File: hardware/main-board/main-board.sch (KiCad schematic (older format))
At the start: 92 parts, among them J1 BARREL_JACK, J2 CONN_01X10, J3 CONN_01X10, J4 USB_OTG, J5 CONN_02X05, J6 SMA, Q1 DDTD113ZC, Q2 DDTD113ZC, Q3 DDTD113ZC, Q4 DDTD113ZC, Q5 DDTD113ZC, Q6 FDB14N30TM, Q7 DDTD113ZC, Q8 DDTD113ZC, Q9 DDTD113ZC, SW1 SW_Push, SW2 SW_Push, SW3 SW_Push, SW4 SW_Push, SW5 SW_DIP_x01, U1 LD1117S33TR, U2 MAX1771, U3 STM32F302C, U4 FGPMMOPA6H, Y1 8MHz, Y2 32.768kHz

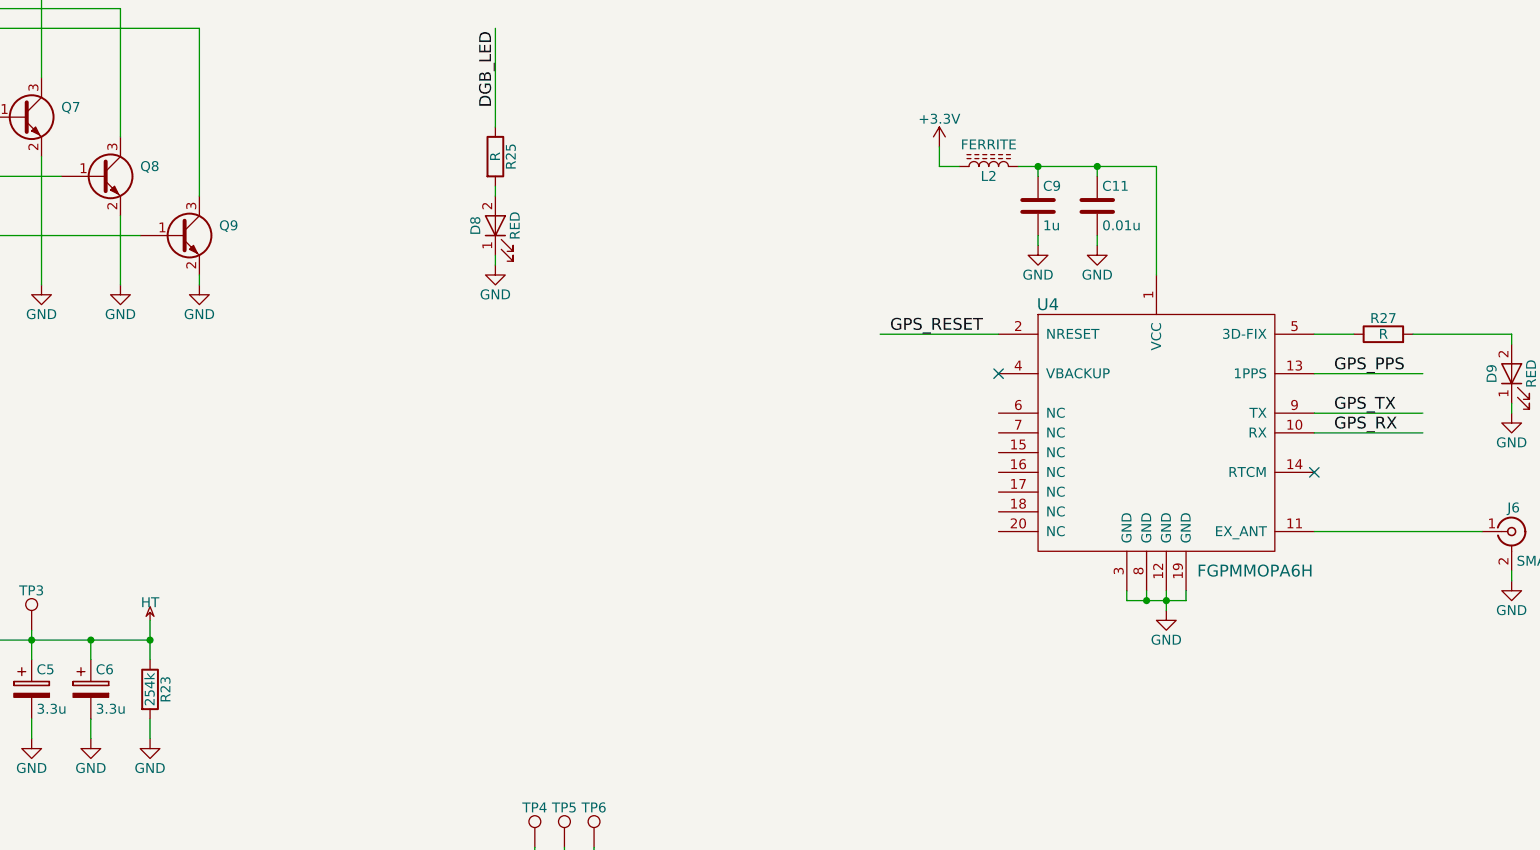
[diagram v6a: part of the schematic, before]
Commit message: Completed BOMs for both boards
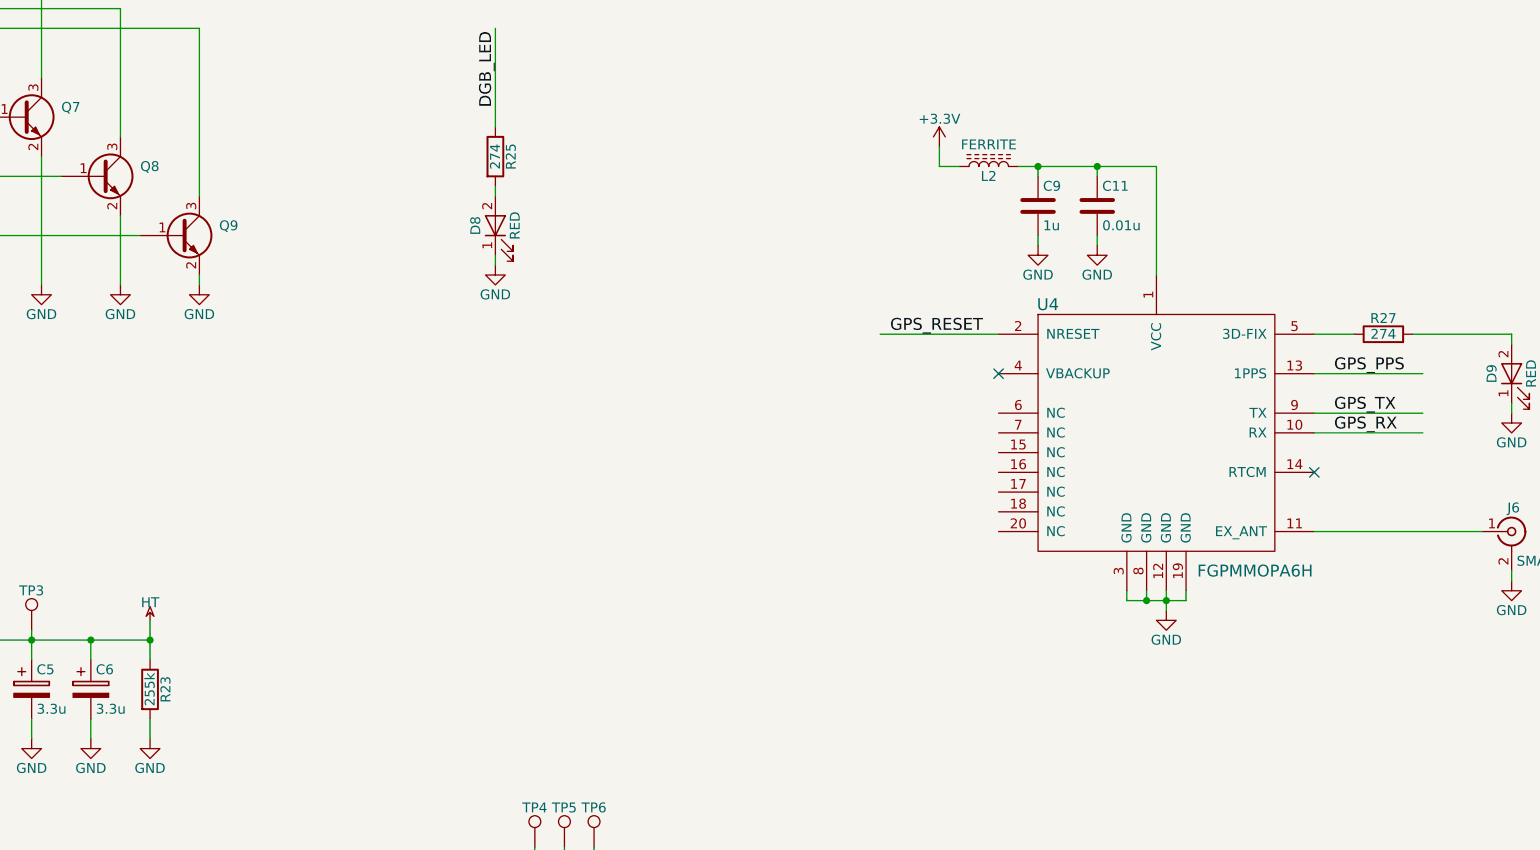
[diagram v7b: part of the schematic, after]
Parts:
- R1, R15, R5: Part (none) -> 311-1.05KCRCT-ND
- R16, R2, R6: Part (none) -> 311-2.43KCRCT-ND
- R17, R3, R7: Part (none) -> 311-499CRCT-ND
- R20, R21: Part (none) -> 311-681KFRCT-ND
- R22: Part (none) -> 311-10.7KFRCT-ND
- R23: value 254k -> 255k; Part (none) -> 311-255KFRCT-ND
- R25, R27: value R -> 274; Part (none) -> 311-274CRCT-ND
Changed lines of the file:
@@
 F 3 "" H 7150 8600 50  0001 C CNN
 F 4 "DigiKey" H 7150 8600 60  0001 C CNN "Source"
+F 5 "311-681KFRCT-ND" H 7150 8600 60  0001 C CNN "Part"
 	1    7150 8600
 	1    0    0    -1
@@
 F 3 "" H 7150 9000 50  0001 C CNN
 F 4 "DigiKey" H 7150 9000 60  0001 C CNN "Source"
+F 5 "311-681KFRCT-ND" H 7150 9000 60  0001 C CNN "Part"
 	1    7150 9000
 	1    0    0    -1
@@
 F 3 "" H 7150 9400 50  0001 C CNN
 F 4 "DigiKey" H 7150 9400 60  0001 C CNN "Source"
+F 5 "311-10.7KFRCT-ND" H 7150 9400 60  0001 C CNN "Part"
 	1    7150 9400
 	1    0    0    -1
@@
 P 8150 8600
 F 0 "R23" V 8230 8600 50  0000 C CNN
-F 1 "254k" V 8150 8600 50  0000 C CNN
+F 1 "255k" V 8150 8600 50  0000 C CNN
 F 2 "Resistors_SMD:R_1206" V 8080 8600 50  0001 C CNN
 F 3 "" H 8150 8600 50  0001 C CNN
 F 4 "DigiKey" H 8150 8600 60  0001 C CNN "Source"
+F 5 "311-255KFRCT-ND" H 8150 8600 60  0001 C CNN "Part"
 	1    8150 8600
 	1    0    0    -1
@@
 P 9900 5900
 F 0 "R25" V 9980 5900 50  0000 C CNN
-F 1 "R" V 9900 5900 50  0000 C CNN
+F 1 "274" V 9900 5900 50  0000 C CNN
 F 2 "Resistors_SMD:R_0805" V 9830 5900 50  0001 C CNN
 F 3 "" H 9900 5900 50  0001 C CNN
 F 4 "DigiKey" H 9900 5900 60  0001 C CNN "Source"
+F 5 "311-274CRCT-ND" H 9900 5900 60  0001 C CNN "Part"
 	1    9900 5900
 	1    0    0    -1
@@
 F 3 "" H 1400 4350 50  0001 C CNN
 F 4 "DigiKey" H 1400 4350 60  0001 C CNN "Source"
+F 5 "311-1.05KCRCT-ND" H 1400 4350 60  0001 C CNN "Part"
 	1    1400 4350
 	0    -1   -1   0
@@
 F 3 "" H 1400 4550 50  0001 C CNN
 F 4 "DigiKey" H 1400 4550 60  0001 C CNN "Source"
+F 5 "311-2.43KCRCT-ND" H 1400 4550 60  0001 C CNN "Part"
 	1    1400 4550
 	0    -1   -1   0
@@
 F 3 "" H 1400 4750 50  0001 C CNN
 F 4 "DigiKey" H 1400 4750 60  0001 C CNN "Source"
+F 5 "311-499CRCT-ND" H 1400 4750 60  0001 C CNN "Part"
 	1    1400 4750
 	0    -1   -1   0
@@
 P 14400 6800
 F 0 "R27" V 14480 6800 50  0000 C CNN
-F 1 "R" V 14400 6800 50  0000 C CNN
+F 1 "274" V 14400 6800 50  0000 C CNN
 F 2 "Resistors_SMD:R_0805" V 14330 6800 50  0001 C CNN
 F 3 "" H 14400 6800 50  0001 C CNN
 F 4 "DigiKey" H 14400 6800 60  0001 C CNN "Source"
+F 5 "311-274CRCT-ND" H 14400 6800 60  0001 C CNN "Part"
 	1    14400 6800
 	0    -1   -1   0
@@
 F 3 "" H 3500 4350 50  0001 C CNN
 F 4 "DigiKey" H 3500 4350 60  0001 C CNN "Source"
+F 5 "311-1.05KCRCT-ND" H 3500 4350 60  0001 C CNN "Part"
 	1    3500 4350
 	0    -1   -1   0
@@
 F 3 "" H 5600 4350 50  0001 C CNN
 F 4 "DigiKey" H 5600 4350 60  0001 C CNN "Source"
+F 5 "311-1.05KCRCT-ND" H 5600 4350 60  0001 C CNN "Part"
 	1    5600 4350
 	0    -1   -1   0
@@
 F 3 "" H 3500 4550 50  0001 C CNN
 F 4 "DigiKey" H 3500 4550 60  0001 C CNN "Source"
+F 5 "311-2.43KCRCT-ND" H 3500 4550 60  0001 C CNN "Part"
 	1    3500 4550
 	0    -1   -1   0
@@
 F 3 "" H 3500 4750 50  0001 C CNN
 F 4 "DigiKey" H 3500 4750 60  0001 C CNN "Source"
+F 5 "311-499CRCT-ND" H 3500 4750 60  0001 C CNN "Part"
 	1    3500 4750
 	0    -1   -1   0
@@
 F 3 "" H 5600 4550 50  0001 C CNN
 F 4 "DigiKey" H 5600 4550 60  0001 C CNN "Source"
+F 5 "311-2.43KCRCT-ND" H 5600 4550 60  0001 C CNN "Part"
 	1    5600 4550
 	0    -1   -1   0
@@
 F 3 "" H 5600 4750 50  0001 C CNN
 F 4 "DigiKey" H 5600 4750 60  0001 C CNN "Source"
+F 5 "311-499CRCT-ND" H 5600 4750 60  0001 C CNN "Part"
 	1    5600 4750
 	0    -1   -1   0

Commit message: Fixed HV5522 footprint on tube board.  Increased size of IN-14 through holes.  Fixed footprint for MOSFET in HV boost circuit.  Fixed hole size for battery holder footprint.
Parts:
- Q6: footprint TO_SOT_Packages_SMD:TO-252-2Lead -> TO_SOT_Packages_SMD:TO-263-2
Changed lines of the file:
@@
 F 0 "Q6" H 6500 8650 50  0000 L CNN
 F 1 "FDB14N30TM" H 6500 8550 50  0000 L CNN
-F 2 "TO_SOT_Packages_SMD:TO-252-2Lead" H 6500 8700 50  0001 C CNN
+F 2 "TO_SOT_Packages_SMD:TO-263-2" H 6500 8700 50  0001 C CNN
 F 3 "" H 6300 8600 50  0001 C CNN
 F 4 "DigiKey" H 6300 8600 60  0001 C CNN "Source"
